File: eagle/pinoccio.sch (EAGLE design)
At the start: 48 parts, among them Q1 16MHz, Q2 32.768k, Q4 MOSFET-PCHANNEL, Q5 TRANSISTOR-NPN-DUAL, U1 MCP73831, U2 3.3V, U4 ATMEGA128RFA1, X1 USB-MICROB, Y2 ANTENNA2SMD5

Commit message: Updated datasheet to dual package transistor.
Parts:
- R4: device SparkFun:RESISTOR0603-RES -> SparkFun:RESISTOR0402-RES
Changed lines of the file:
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@@
 <grid distance="0.1" unitdist="inch" unit="inch" style="lines" multiple="1" display="no" altdistance="0.01" altunitdist="inch" altunit="inch"/>
 <layers>
-<layer number="1" name="Top" color="4" fill="1" visible="no" active="no"/>
-<layer number="2" name="Route2" color="1" fill="3" visible="no" active="no"/>
-<layer number="3" name="Route3" color="4" fill="3" visible="no" active="no"/>
-<layer number="4" name="Route4" color="1" fill="4" visible="no" active="no"/>
-<layer number="5" name="Route5" color="4" fill="4" visible="no" active="no"/>
-<layer number="6" name="Route6" color="1" fill="8" visible="no" active="no"/>
-<layer number="7" name="Route7" color="4" fill="8" visible="no" active="no"/>
-<layer number="8" name="Route8" color="1" fill="2" visible="no" active="no"/>
-<layer number="9" name="Route9" color="4" fill="2" visible="no" active="no"/>
-<layer number="10" name="Route10" color="1" fill="7" visible="no" active="no"/>
-<layer number="11" name="Route11" color="4" fill="7" visible="no" active="no"/>
-<layer number="12" name="Route12" color="1" fill="5" visible="no" active="no"/>
-<layer number="13" name="Route13" color="4" fill="5" visible="no" active="no"/>
-<layer number="14" name="Route14" color="1" fill="6" visible="no" active="no"/>
-<layer number="15" name="Route15" color="4" fill="6" visible="no" active="no"/>
-<layer number="16" name="Bottom" color="1" fill="1" visible="no" active="no"/>
-<layer number="17" name="Pads" color="2" fill="1" visible="no" active="no"/>
-<layer number="18" name="Vias" color="2" fill="1" visible="no" active="no"/>
-<layer number="19" name="Unrouted" color="6" fill="1" visible="no" active="no"/>
-<layer number="20" name="Dimension" color="6" fill="1" visible="no" active="no"/>
-<layer number="21" name="tPlace" color="16" fill="1" visible="no" active="no"/>
-<layer number="22" name="bPlace" color="14" fill="1" visible="no" active="no"/>
-<layer number="23" name="tOrigins" color="15" fill="1" visible="no" active="no"/>
-<layer number="24" name="bOrigins" color="15" fill="1" visible="no" active="no"/>
-<layer number="25" name="tNames" color="7" fill="1" visible="no" active="no"/>
-<layer number="26" name="bNames" color="7" fill="1" visible="no" active="no"/>
-<layer number="27" name="tValues" color="7" fill="1" visible="no" active="no"/>
-<layer number="28" name="bValues" color="7" fill="1" visible="no" active="no"/>
+<layer number="1" name="Top" color="4" fill="1" visible="yes" active="no"/>
+<layer number="2" name="Route2" color="1" fill="3" visible="yes" active="no"/>
+<layer number="3" name="Route3" color="4" fill="3" visible="yes" active="no"/>
+<layer number="4" name="Route4" color="1" fill="4" visible="yes" active="no"/>
+<layer number="5" name="Route5" color="4" fill="4" visible="yes" active="no"/>
+<layer number="6" name="Route6" color="1" fill="8" visible="yes" active="no"/>
+<layer number="7" name="Route7" color="4" fill="8" visible="yes" active="no"/>
+<layer number="8" name="Route8" color="1" fill="2" visible="yes" active="no"/>
+<layer number="9" name="Route9" color="4" fill="2" visible="yes" active="no"/>
+<layer number="10" name="Route10" color="1" fill="7" visible="yes" active="no"/>
+<layer number="11" name="Route11" color="4" fill="7" visible="yes" active="no"/>
+<layer number="12" name="Route12" color="1" fill="5" visible="yes" active="no"/>
+<layer number="13" name="Route13" color="4" fill="5" visible="yes" active="no"/>
+<layer number="14" name="Route14" color="1" fill="6" visible="yes" active="no"/>
+<layer number="15" name="Route15" color="4" fill="6" visible="yes" active="no"/>
+<layer number="16" name="Bottom" color="1" fill="1" visible="yes" active="no"/>
+<layer number="17" name="Pads" color="2" fill="1" visible="yes" active="no"/>
+<layer number="18" name="Vias" color="2" fill="1" visible="yes" active="no"/>
+<layer number="19" name="Unrouted" color="6" fill="1" visible="yes" active="no"/>
+<layer number="20" name="Dimension" color="6" fill="1" visible="yes" active="no"/>
+<layer number="21" name="tPlace" color="16" fill="1" visible="yes" active="no"/>
+<layer number="22" name="bPlace" color="14" fill="1" visible="yes" active="no"/>
+<layer number="23" name="tOrigins" color="15" fill="1" visible="yes" active="no"/>
+<layer number="24" name="bOrigins" color="15" fill="1" visible="yes" active="no"/>
+<layer number="25" name="tNames" color="7" fill="1" visible="yes" active="no"/>
+<layer number="26" name="bNames" color="7" fill="1" visible="yes" active="no"/>
+<layer number="27" name="tValues" color="7" fill="1" visible="yes" active="no"/>
+<layer number="28" name="bValues" color="7" fill="1" visible="yes" active="no"/>
 <layer number="29" name="tStop" color="5" fill="1" visible="no" active="no"/>
 <layer number="30" name="bStop" color="7" fill="6" visible="no" active="no"/>
@@
 <layer number="35" name="tGlue" color="7" fill="4" visible="no" active="no"/>
 <layer number="36" name="bGlue" color="7" fill="5" visible="no" active="no"/>
-<layer number="37" name="tTest" color="7" fill="1" visible="no" active="no"/>
-<layer number="38" name="bTest" color="7" fill="1" visible="no" active="no"/>
+<layer number="37" name="tTest" color="7" fill="1" visible="yes" active="no"/>
+<layer number="38" name="bTest" color="7" fill="1" visible="yes" active="no"/>
 <layer number="39" name="tKeepout" color="4" fill="11" visible="no" active="no"/>
 <layer number="40" name="bKeepout" color="1" fill="11" visible="no" active="no"/>
@@
 <layer number="44" name="Drills" color="7" fill="1" visible="no" active="no"/>
 <layer number="45" name="Holes" color="7" fill="1" visible="no" active="no"/>
-<layer number="46" name="Milling" color="3" fill="1" visible="no" active="no"/>
-<layer number="47" name="Measures" color="7" fill="1" visible="no" active="no"/>
-<layer number="48" name="Document" color="7" fill="1" visible="no" active="no"/>
-<layer number="49" name="Reference" color="7" fill="1" visible="no" active="no"/>
-<layer number="50" name="dxf" color="7" fill="1" visible="no" active="no"/>
-<layer number="51" name="tDocu" color="6" fill="1" visible="no" active="no"/>
-<layer number="52" name="bDocu" color="7" fill="1" visible="no" active="no"/>
-<layer number="53" name="tGND_GNDA" color="7" fill="9" visible="no" active="no"/>
-<layer number="54" name="bGND_GNDA" color="1" fill="9" visible="no" active="no"/>
-<layer number="56" name="wert" color="7" fill="1" visible="no" active="no"/>
+<layer number="46" name="Milling" color="3" fill="1" visible="yes" active="no"/>
+<layer number="47" name="Measures" color="7" fill="1" visible="yes" active="no"/>
+<layer number="48" name="Document" color="7" fill="1" visible="yes" active="no"/>
+<layer number="49" name="Reference" color="7" fill="1" visible="yes" active="no"/>
+<layer number="50" name="dxf" color="7" fill="1" visible="yes" active="no"/>
+<layer number="51" name="tDocu" color="6" fill="1" visible="yes" active="no"/>
+<layer number="52" name="bDocu" color="7" fill="1" visible="yes" active="no"/>
+<layer number="53" name="tGND_GNDA" color="7" fill="9" visible="yes" active="no"/>
+<layer number="54" name="bGND_GNDA" color="1" fill="9" visible="yes" active="no"/>
+<layer number="56" name="wert" color="7" fill="1" visible="yes" active="no"/>
 <layer number="91" name="Nets" color="2" fill="1" visible="yes" active="yes"/>
 <layer number="92" name="Busses" color="1" fill="1" visible="yes" active="yes"/>
@@
 <part name="U$5" library="SparkFun" deviceset="FIDUCIAL" device="1X2"/>
 <part name="U1" library="SparkFun" deviceset="MCP73831" device="SMD" value="MCP73831"/>
-<part name="R4" library="SparkFun" deviceset="RESISTOR" device="0603-RES" value="2K"/>
+<part name="R4" library="SparkFun" deviceset="RESISTOR" device="0402-RES" value="2K"/>
 <part name="GND14" library="supply1" deviceset="GND" device=""/>
 <part name="GND17" library="supply1" deviceset="GND" device=""/>

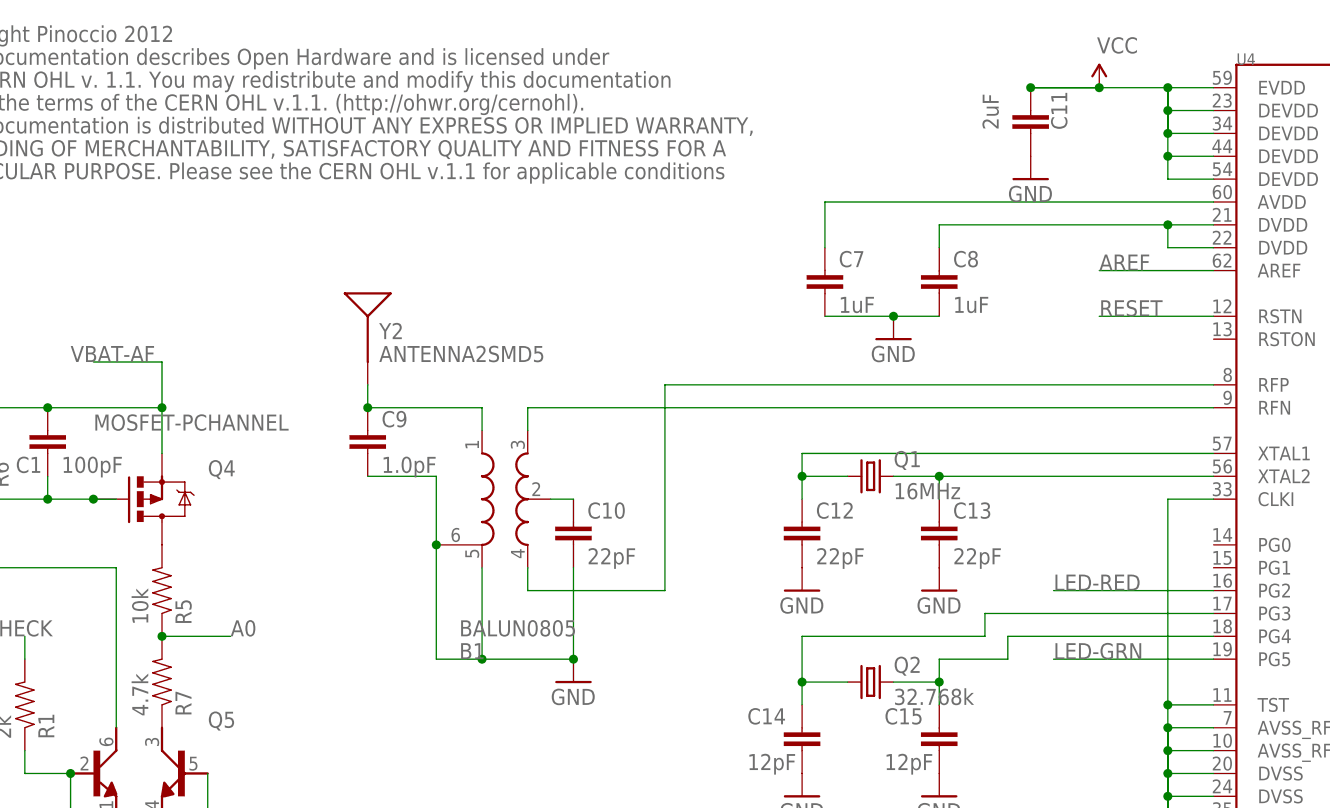
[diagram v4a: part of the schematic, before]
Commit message: Update package for right-angle switch, make minor changes as recommended in Atmel App Note AVR2044
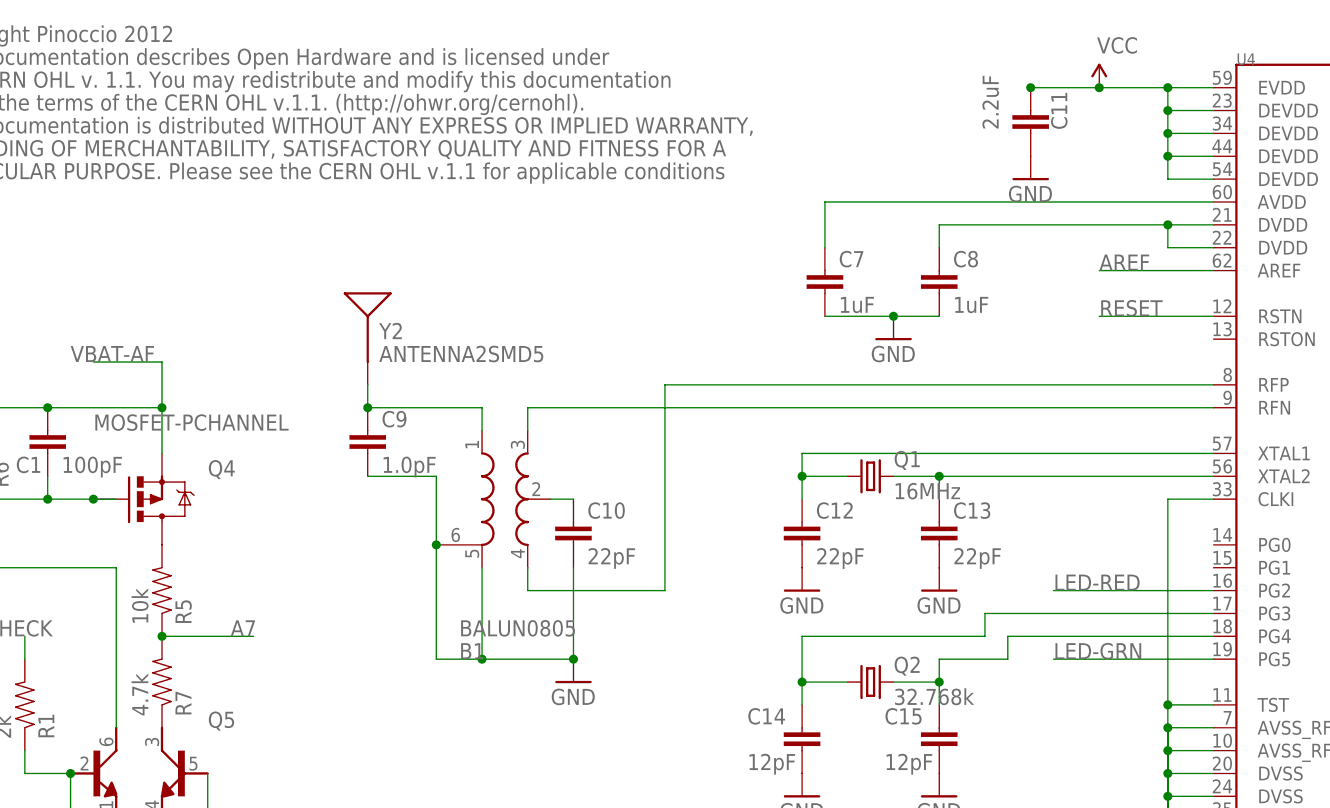
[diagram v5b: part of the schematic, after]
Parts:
- C11: value 2uF -> 2.2uF
- S2: device SparkFun:SWITCH-SPSTSMD2 -> Pinoccio:SWITCH-SPSTSMD2
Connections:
- net A0: no longer R5.1, R7.2
- net A7: now also R5.1, R7.2
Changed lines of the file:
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@@
 <part name="GND21" library="supply1" deviceset="GND" device=""/>
 <part name="F1" library="SparkFun" deviceset="PTC" device="SMD"/>
-<part name="S2" library="SparkFun" deviceset="SWITCH-SPST" device="SMD2" value="SPST"/>
+<part name="S2" library="Pinoccio" deviceset="SWITCH-SPST" device="SMD2" value="SPST"/>
 <part name="U$4" library="SparkFun" deviceset="FIDUCIAL" device="1X2"/>
 <part name="U$5" library="SparkFun" deviceset="FIDUCIAL" device="1X2"/>
@@
 <part name="R10" library="SparkFun" deviceset="RESISTOR" device="0402-RES" value="68"/>
 <part name="P+3" library="SparkFun" deviceset="VCC" device=""/>
-<part name="C11" library="SparkFun" deviceset="CAP" device="0402-CAP" value="2uF"/>
+<part name="C11" library="SparkFun" deviceset="CAP" device="0402-CAP" value="2.2uF"/>
 <part name="GND9" library="SparkFun" deviceset="GND" device=""/>
 <part name="JP1" library="Pinoccio" deviceset="JUMPER-2" device="PTH" value="Switch"/>
@@
 <pinref part="P+3" gate="1" pin="VCC"/>
 <wire x1="139.7" y1="177.8" x2="132.08" y2="177.8" width="0.1524" layer="91"/>
-<wire x1="132.08" y1="177.8" x2="124.46" y2="177.8" width="0.1524" layer="91"/>
 <wire x1="144.78" y1="167.64" x2="139.7" y2="167.64" width="0.1524" layer="91"/>
 <wire x1="139.7" y1="167.64" x2="139.7" y2="170.18" width="0.1524" layer="91"/>
@@
 <wire x1="139.7" y1="177.8" x2="144.78" y2="177.8" width="0.1524" layer="91"/>
 <junction x="139.7" y="175.26"/>
-<wire x1="139.7" y1="177.8" x2="139.7" y2="172.72" width="0.1524" layer="91"/>
 <junction x="139.7" y="177.8"/>
 <pinref part="C11" gate="G$1" pin="1"/>
@@
 <label x="223.52" y="104.14" size="1.778" layer="95"/>
 </segment>
-<segment>
-<pinref part="R5" gate="G$1" pin="1"/>
-<pinref part="R7" gate="G$1" pin="2"/>
-<junction x="27.94" y="116.84"/>
-<wire x1="27.94" y1="116.84" x2="35.56" y2="116.84" width="0.1524" layer="91"/>
-<label x="35.56" y="116.84" size="1.778" layer="95"/>
-</segment>
 </net>
 <net name="A1" class="0">
@@
 <label x="223.52" y="86.36" size="1.778" layer="95"/>
 </segment>
+<segment>
+<pinref part="R5" gate="G$1" pin="1"/>
+<pinref part="R7" gate="G$1" pin="2"/>
+<wire x1="27.94" y1="116.84" x2="38.1" y2="116.84" width="0.1524" layer="91"/>
+<junction x="27.94" y="116.84"/>
+<label x="35.56" y="116.84" size="1.778" layer="95"/>
+</segment>
 </net>
 <net name="N$2" class="0">
@@
 </segment>
 </net>
-<net name="N$13" class="0">
-<segment>
-<pinref part="R7" gate="G$1" pin="1"/>
-<pinref part="Q5" gate="G$1" pin="2C"/>
-</segment>
-</net>
 <net name="N$7" class="0">
 <segment>
@@
 </segment>
 </net>
+<net name="N$14" class="0">
+<segment>
+<pinref part="Q5" gate="G$1" pin="2C"/>
+<pinref part="R7" gate="G$1" pin="1"/>
+</segment>
+</net>

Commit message: Version 0.6
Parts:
- removed U$4, U$5: FIDUCIAL1X2, SparkFun:FIDUCIAL1X2
- added C16, C17: 22pF, Pinoccio:CAP0402-CAP
- added C18: 1.0uF, Pinoccio:CAP0402-CAP
- added C19: 100nF, Pinoccio:CAP0402-CAP
- added D1: Green, Pinoccio:LED0603
- added IC1: ATMEGA16U2QFN32, Pinoccio:ATMEGA16U2QFN32
- added J1: AVR_SPI_PRG_6, Pinoccio:AVR_SPI_PRG_6
- added JP3, JP5: FIDUCIALUFIDUCIAL, Pinoccio:FIDUCIALUFIDUCIAL
- added L1: BML15H0603, Pinoccio:BML15H0603
- added Q3: 16MHz, BeanLabs:CRYSTALABM10
- added R13, R2: VARISTOR0402, Pinoccio:VARISTOR0402
- added R14, R15, R17: 1k, Pinoccio:RESISTOR0402-RES
- added R18: 1K, Pinoccio:RESISTOR0402-RES
- B1: device SparkFun:BALUN0805 -> Pinoccio:BALUN0805
- BATT: value JST Battery -> JST Bat
- C1, C10, C11, C12, C13, C14, C15, C2, C3, C4, C5, C6, C7, C8, C9: device SparkFun:CAP0402-CAP -> Pinoccio:CAP0402-CAP
- D2: device SparkFun:LED0603 -> Pinoccio:LED0603
- JP4: device SparkFun:AVR_SPI_PRG_6PTH -> Pinoccio:AVR_SPI_PRG_6PTH
- R1, R11, R12, R4, R5, R6, R7: device SparkFun:RESISTOR0402-RES -> Pinoccio:RESISTOR0402-RES
- R10, R9: value 68 -> 22; device SparkFun:RESISTOR0402-RES -> Pinoccio:RESISTOR0402-RES
- R3: value 470 -> 1k; device SparkFun:RESISTOR0402-RES -> Pinoccio:RESISTOR0402-RES
- R8: value 1.5K -> 1k; device SparkFun:RESISTOR0402-RES -> Pinoccio:RESISTOR0402-RES
- U$1: value LED-BICOLOR -> LED-RGBPLCC4; device Pinoccio:LED-BICOLOR -> Pinoccio:LED-RGBPLCC4
- U1: device SparkFun:MCP73831SMD -> Pinoccio:MCP73831
- X1: device SparkFun:USB-MICROB -> Pinoccio:USB-MICROB
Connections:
- net N$1 renamed RFN
- net N$52 renamed RFP
- removed net USBENABLE: R8.1, U4.PD5
- new net LED-BLU: R18.1, U4.PB4
- new net N$1: R12.2, U$1.R-C
- new net N$13: B1.RFGND@2, C10.1
- new net N$19: C16.1, IC1.XTAL2/PC0, Q3.1
- new net N$21: C17.1, IC1.XTAL1, Q3.2
- new net N$23: C18.1, IC1.AVCC, IC1.UCAP, IC1.VCC
- new net N$24: C19.2, IC1.PD7(INT7/HWB/AIN6/T0), R17.2
- new net N$55: IC1./RESET(PC1), J1.5
- new net N$56: IC1.PB3(PDO/MISO/PCINT3), J1.1
- new net N$57: IC1.PB2(PDI/MOSI/PCINT2), J1.4
- new net N$58: IC1.PB1(SCK/PCINT1), J1.3
- new net N$59: IC1.PD4(INT5/AIN3), R14.1
- new net N$62: D1.C, R14.2
- net D2: now also U4.PB7; no longer U4.PB4
- net D3: now also U4.PE2; no longer U4.PB5
- net D4: now also U4.PE3; no longer U4.PB6
- net D5: now also U4.PE4; no longer U4.PB7
- net GND: now also C16.2, C17.2, C18.2, IC1.GND, IC1.UGND, J1.6, L1.1, R17.1, U1.GND, U4.AVSS@PADDLE; no longer U$1.3, U$1.4, U1.VSS
- net LED-GRN: now also U4.PB6; no longer U4.PG5
- net LED-RED: now also U4.PB5; no longer U4.PG2
- net N$2: now also R2.1, R9.1, X1.D-; no longer B1.GND@2, C10.1
- net N$43: now also R13.1
- net N$5: now also U$1.G-C; no longer U$1.1
- net N$6: now also R18.2, U$1.B-C; no longer R12.2, U$1.2
- net N$9: now also L1.2, R13.2, R2.2; no longer R8.2, R9.1, X1.D-
- net RESET: now also C19.1
- net RX0: now also IC1.PD3(INT3/TXD1), R15.1, R15.2
- net TX0: now also IC1.PD2(INT2/AIN1/RXD1), R8.1, R8.2
- net USBD+: now also IC1.D+; no longer U4.PE4
- net USBD-: now also IC1.D-; no longer U4.PE3
- net USB_VIN: now also D1.A, IC1.UVCC, J1.2, JP-L.1; no longer JP-L.3
- net VBAT-AF: now also JP-L.3
- net VCC: now also U$1.A; no longer JP-L.1
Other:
- note added: "0.6"
- note added: "~"
- note removed: "0.5"
- note removed: "Eric Jennings"
- note removed: "Pinoccio"
- moved on the sheet: B1, BATT, C1, C10, C12, C13, C14, C15, C2, C3, C4, C5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

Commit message: Update to latest v0.6
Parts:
- removed C1: 100pF, Pinoccio:CAP0402-CAP
- removed Q4: MOSFET-PCHANNEL, Pinoccio:MOSFET-PCHANNELSMD
- removed Q5: TRANSISTOR-NPN-DUAL, Pinoccio:TRANSISTOR-NPN-DUAL
- removed R1: 2k, Pinoccio:RESISTOR0402-RES
- added D3: DIODE-SCHOTTKY, Pinoccio:DIODE-SCHOTTKY
- added U$2: MOSFET-DUAL-N-P, Pinoccio:MOSFET-DUAL-N-P
- JP-L, JP-R: value M16 -> M162MM; device SparkFun:M16 -> Pinoccio:M162MM
- R11, R12, R18: value 1K -> 470
- R6: value 100k -> 1M
- R7: value 4.7k -> 40k
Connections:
- removed net N$51: C1.2, Q4.G, Q5.1C, R6.1
- net A7: now also D3.C; no longer R5.1, R7.2
- net BATTCHECK: now also U$2G$N1.G; no longer R1.2
- net GND: now also R7.1, U$2G$N1.S; no longer Q5.1E, Q5.2E
- net N$14: now also D3.A, R5.1, R7.2; no longer Q5.2C, R7.1
- net N$3: now also U$2G$P2.D; no longer Q4.D
- net N$7: now also R6.1, U$2G$N1.D, U$2G$P2.G; no longer Q5.1B, Q5.2B, R1.1
- net VBAT-AF: now also U$2G$P2.S; no longer C1.1, Q4.S
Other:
- moved on the sheet: JP-L, JP-R, R5, R6, R7
